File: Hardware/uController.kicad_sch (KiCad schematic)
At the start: 1 part

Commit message: included psu on pcb
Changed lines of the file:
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@@
     (company "ncAudio")
+  )
+  (hierarchical_label "EN" (shape input) (at 86.36 113.03 180)
+    (effects (font (size 1.27 1.27)) (justify right))
+  )
+  (hierarchical_label "EN" (shape input) (at 86.36 109.22 180)
+    (effects (font (size 1.27 1.27)) (justify right))
+  )
+  (hierarchical_label "SPI" (shape input) (at 86.36 101.6 180)
+    (effects (font (size 1.27 1.27)) (justify right))
+  )
+  (hierarchical_label "DT" (shape input) (at 86.36 123.19 180)
+    (effects (font (size 1.27 1.27)) (justify right))
+  )
+  (hierarchical_label "PWR" (shape input) (at 86.36 97.79 180)
+    (effects (font (size 1.27 1.27)) (justify right))
+  )
+  (hierarchical_label "GND" (shape input) (at 86.36 129.54 180)
+    (effects (font (size 1.27 1.27)) (justify right))
+  )
+  (hierarchical_label "I2C_0" (shape input) (at 86.36 105.41 180)
+    (effects (font (size 1.27 1.27)) (justify right))
+  )
+  (hierarchical_label "I2C_1" (shape input) (at 86.36 116.84 180)
+    (effects (font (size 1.27 1.27)) (justify right))
+  )
+  (hierarchical_label "3V3_0" (shape input) (at 86.36 93.98 180)
+    (effects (font (size 1.27 1.27)) (justify right))
+  )
+  (hierarchical_label "CLK" (shape input) (at 86.36 125.73 180)
+    (effects (font (size 1.27 1.27)) (justify right))
+  )
+  (hierarchical_label "SW_RE" (shape input) (at 86.36 120.65 180)
+    (effects (font (size 1.27 1.27)) (justify right))
   )
   (symbol (lib_id "RF_Module:ESP32-S2-WROVER") (at 146.05 99.06 0) (unit 1)

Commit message: fixes for hierarchical sheets
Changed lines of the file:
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@@
     (company "ncAudio")
+  )
+  (hierarchical_label "bat_sense" (shape input) (at 86.36 90.17 180)
+    (effects (font (size 1.27 1.27)) (justify right))
   )
   (hierarchical_label "EN" (shape input) (at 86.36 113.03 180)

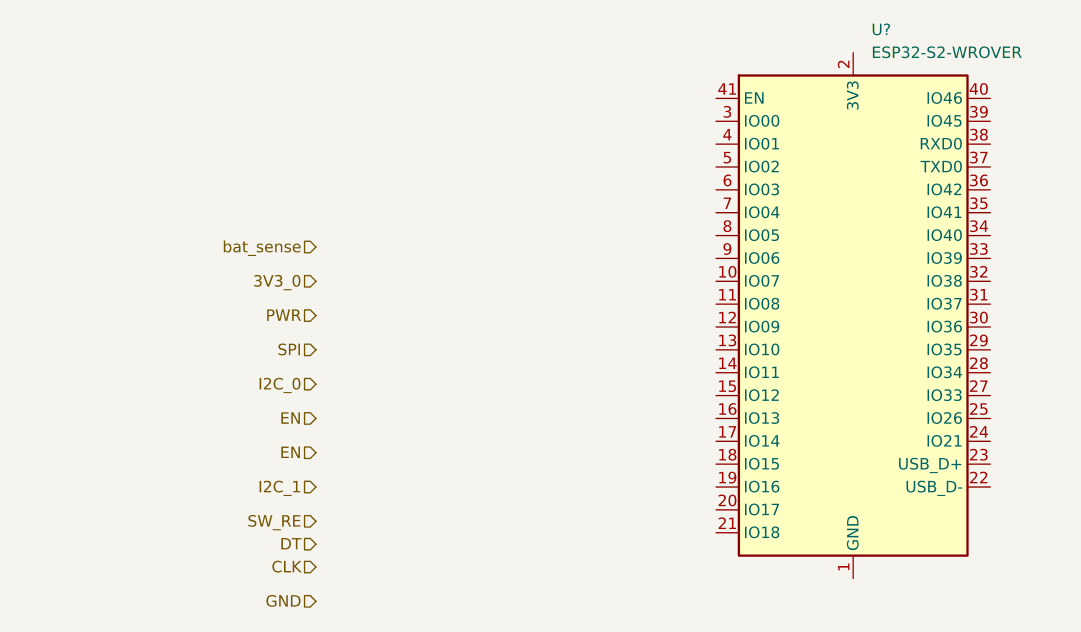
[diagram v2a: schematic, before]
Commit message: added hierrarchial labels
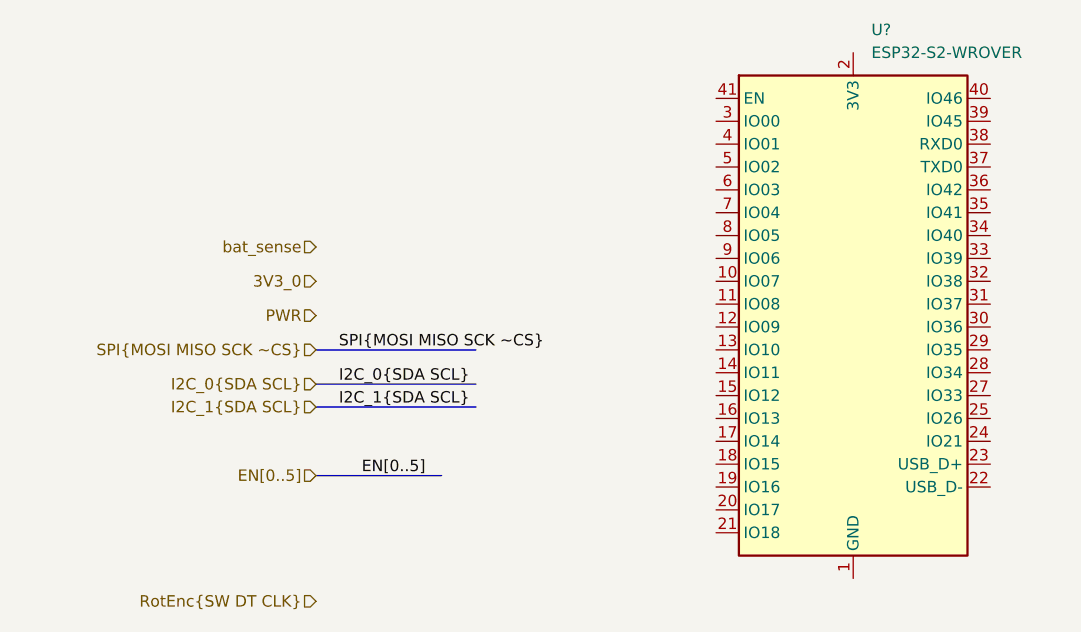
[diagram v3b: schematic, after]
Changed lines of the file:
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@@
     (company "ncAudio")
+  )
+  (bus (pts (xy 86.36 107.95) (xy 104.14 107.95))
+    (stroke (width 0) (type default) (color 0 0 0 0))
+  )
+  (bus (pts (xy 86.36 115.57) (xy 100.33 115.57))
+    (stroke (width 0) (type default) (color 0 0 0 0))
+  )
+  (bus (pts (xy 86.36 101.6) (xy 104.14 101.6))
+    (stroke (width 0) (type default) (color 0 0 0 0))
+  )
+  (bus (pts (xy 86.36 105.41) (xy 104.14 105.41))
+    (stroke (width 0) (type default) (color 0 0 0 0))
+  )
+  (label "SPI{MOSI MISO SCK ~CS}" (at 88.9 101.6 0)
+    (effects (font (size 1.27 1.27)) (justify left bottom))
+  )
+  (label "EN[0..5]" (at 91.44 115.57 0)
+    (effects (font (size 1.27 1.27)) (justify left bottom))
+  )
+  (label "I2C_0{SDA SCL}" (at 88.9 105.41 0)
+    (effects (font (size 1.27 1.27)) (justify left bottom))
+  )
+  (label "I2C_1{SDA SCL}" (at 88.9 107.95 0)
+    (effects (font (size 1.27 1.27)) (justify left bottom))
   )
   (hierarchical_label "bat_sense" (shape input) (at 86.36 90.17 180)
     (effects (font (size 1.27 1.27)) (justify right))
   )
-  (hierarchical_label "EN" (shape input) (at 86.36 113.03 180)
-    (effects (font (size 1.27 1.27)) (justify right))
-  )
-  (hierarchical_label "EN" (shape input) (at 86.36 109.22 180)
-    (effects (font (size 1.27 1.27)) (justify right))
-  )
-  (hierarchical_label "SPI" (shape input) (at 86.36 101.6 180)
-    (effects (font (size 1.27 1.27)) (justify right))
-  )
-  (hierarchical_label "DT" (shape input) (at 86.36 123.19 180)
+  (hierarchical_label "SPI{MOSI MISO SCK ~CS}" (shape input) (at 86.36 101.6 180)
     (effects (font (size 1.27 1.27)) (justify right))
   )
@@
     (effects (font (size 1.27 1.27)) (justify right))
   )
-  (hierarchical_label "GND" (shape input) (at 86.36 129.54 180)
+  (hierarchical_label "RotEnc{SW DT CLK}" (shape input) (at 86.36 129.54 180)
     (effects (font (size 1.27 1.27)) (justify right))
   )
-  (hierarchical_label "I2C_0" (shape input) (at 86.36 105.41 180)
+  (hierarchical_label "I2C_0{SDA SCL}" (shape input) (at 86.36 105.41 180)
     (effects (font (size 1.27 1.27)) (justify right))
   )
-  (hierarchical_label "I2C_1" (shape input) (at 86.36 116.84 180)
+  (hierarchical_label "EN[0..5]" (shape input) (at 86.36 115.57 180)
+    (effects (font (size 1.27 1.27)) (justify right))
+  )
+  (hierarchical_label "I2C_1{SDA SCL}" (shape input) (at 86.36 107.95 180)
     (effects (font (size 1.27 1.27)) (justify right))
   )
@@
     (effects (font (size 1.27 1.27)) (justify right))
   )
-  (hierarchical_label "CLK" (shape input) (at 86.36 125.73 180)
-    (effects (font (size 1.27 1.27)) (justify right))
-  )
-  (hierarchical_label "SW_RE" (shape input) (at 86.36 120.65 180)
-    (effects (font (size 1.27 1.27)) (justify right))
-  )

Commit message: cleaned up busses
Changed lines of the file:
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@@
     (effects (font (size 1.27 1.27)) (justify right))
   )
-  (hierarchical_label "SPI{MOSI MISO SCK ~CS}" (shape input) (at 86.36 101.6 180)
+  (hierarchical_label "SPI{MOSI MISO SCK ~{CS}}" (shape input) (at 86.36 101.6 180)
     (effects (font (size 1.27 1.27)) (justify right))
   )
@@
     (effects (font (size 1.27 1.27)) (justify right))
   )
-  (hierarchical_label "3V3_0" (shape input) (at 86.36 93.98 180)
+  (hierarchical_label "3V3" (shape input) (at 86.36 93.98 180)
     (effects (font (size 1.27 1.27)) (justify right))
   )
